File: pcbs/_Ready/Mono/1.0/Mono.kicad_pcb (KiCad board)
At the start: 2 copper layers, 100 x 45 mm, 36 parts, among them J1 Conn_01x03_Male, J10 Conn_01x02_Pin, J11 Conn_01x02_Pin, J12 Conn_01x02_Pin, J13 Conn_01x03_Pin, J2 Conn_01x02_Pin, J3 Conn_01x02_Pin, J5 Conn_01x04_Pin, J6 Conn_01x03_Male, J7 Conn_01x03_Male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

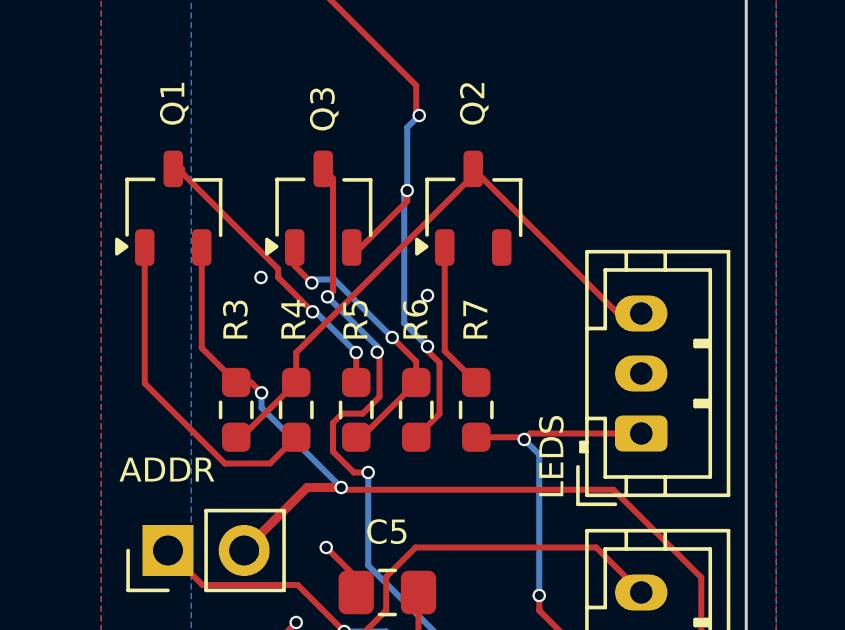
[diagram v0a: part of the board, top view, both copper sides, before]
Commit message: Updated screenshots
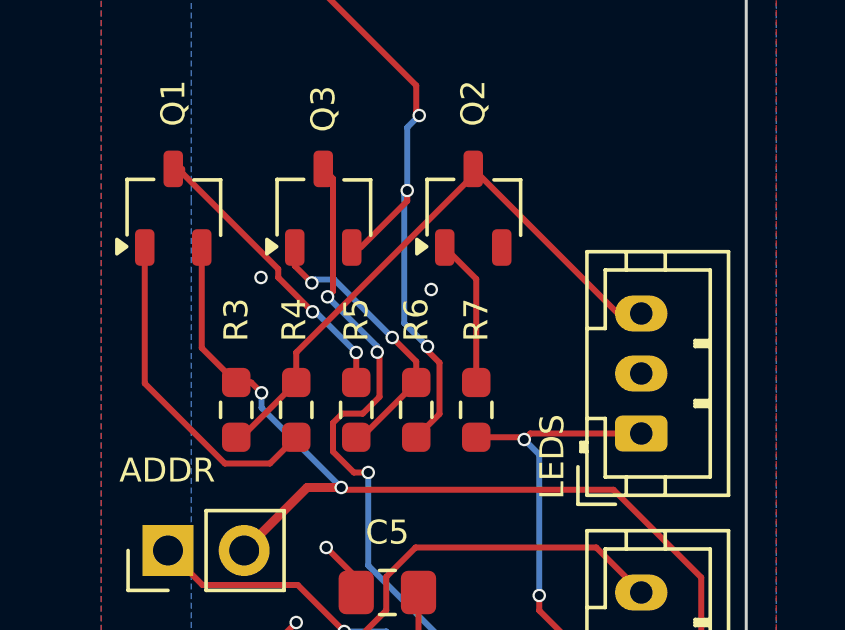
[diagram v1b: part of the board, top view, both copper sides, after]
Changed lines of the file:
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@@
 	)
 	(via
-		(at 175.275 93.1)
+		(at 175.4 92.9)
 		(size 0.45)
 		(drill 0.3)
@@
 	)
 	(segment
-		(start 175.85 94.95)
+		(start 176.9 92.55)
 		(end 176.9 96)
 		(width 0.2)
@@
 	(segment
 		(start 175.85 91.5)
-		(end 175.85 94.95)
-		(width 0.2)
-		(layer "F.Cu")
+		(end 176.9 92.55)
+		(width 0.2)
+		(layer "F.Cu")
